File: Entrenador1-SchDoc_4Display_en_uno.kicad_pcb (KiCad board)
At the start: 2 copper layers, 154.9 x 106.7 mm, 85 parts, among them J11 CON8, J3 ICSP, J5 CON8, J6 CON8, J7 CON8, J9 3vias, P1 CONN_01X04, P10 CONN_01X04, P2 CONN_01X04, P3 CONN_01X05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

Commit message: Changes to be committed: 	modified:   Entrenador1-SchDoc_4Display_en_uno-cache.lib 	modified:   Entrenador1-SchDoc_4Display_en_uno.kicad_pcb 	modified:   Entrenador1-SchDoc_4Display_en_uno.kicad_pcb-bak 	modified:   Entrenador1-SchDoc_4Display_en_uno.sch 	modified:   Entrenador1-SchDoc_4Display_en_uno.sch-bak
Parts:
- moved R20 7.75 mm to (182.8, 60.5), turned to 270 degrees
- moved R26 7.62 mm to (189.6, 38.7), turned to 0 degrees
- moved R1 7.62 mm to (142.0, 106.7), turned to 90 degrees
- moved R17 7.62 mm to (142.9, 60.5), turned to 270 degrees
- moved R18 7.62 mm to (154.9, 60.5), turned to 270 degrees
- moved R19 7.62 mm to (171.8, 60.5), turned to 270 degrees
- moved R2 7.62 mm to (142.0, 109.2), turned to 270 degrees
- moved R21 7.62 mm to (189.6, 57.9), turned to 0 degrees
- moved R22 7.62 mm to (189.6, 42.5), turned to 0 degrees
- moved R23 7.62 mm to (189.6, 61.2), turned to 0 degrees
- moved R24 7.62 mm to (189.6, 46.3), turned to 0 degrees
- moved R25 7.62 mm to (187.3, 49.7), turned to 0 degrees
- moved R27 7.62 mm to (189.6, 54.6), turned to 0 degrees
- moved R28 7.62 mm to (189.6, 64.5), turned to 0 degrees
- moved R29 7.62 mm to (209.8, 63.8), turned to 0 degrees
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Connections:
- R1 pad 1: MCRL -> VDD
- R1 pad 2: VDD -> MCRL
- R17 pad 1: Disp1 -> Net-(Q1-Pad2)
- R17 pad 2: Net-(Q1-Pad2) -> Disp1
- R18 pad 1: Disp2 -> Net-(Q2-Pad2)
- R18 pad 2: Net-(Q2-Pad2) -> Disp2
- R19 pad 1: Disp3 -> Net-(Q3-Pad2)
- R19 pad 2: Net-(Q3-Pad2) -> Disp3
- R2 pad 1: RB4 -> VDD
- R2 pad 2: VDD -> RB4
- R20 pad 1: Disp4 -> Net-(Q4-Pad2)
- R20 pad 2: Net-(Q4-Pad2) -> Disp4
- R21 pad 1: Net-(R21-Pad1) -> /a
- R21 pad 2: /a -> Net-(R21-Pad2)
- R22 pad 1: Net-(R22-Pad1) -> /b
- R22 pad 2: /b -> Net-(R22-Pad2)
- R23 pad 1: Net-(R23-Pad1) -> /c
- R23 pad 2: /c -> Net-(R23-Pad2)
- R24 pad 1: Net-(R24-Pad1) -> /d
- R24 pad 2: /d -> Net-(R24-Pad2)
- R25 pad 1: Net-(R25-Pad1) -> /e
- R25 pad 2: /e -> Net-(R25-Pad2)
- R26 pad 1: Net-(R26-Pad1) -> /f
- R26 pad 2: /f -> Net-(R26-Pad2)
- R27 pad 1: Net-(R27-Pad1) -> /g
- R27 pad 2: /g -> Net-(R27-Pad2)
- R28 pad 1: /DisplayH -> /h
- R28 pad 2: /h -> /DisplayH
- R29 pad 1: GNDD -> /Display_A
- R29 pad 2: /Display_A -> GNDD
- R3 pad 1: Net-(D2-Pad1) -> RD0
- R3 pad 2: RD0 -> Net-(D2-Pad1)
- R30 pad 1: GNDD -> /Display_B
- R30 pad 2: /Display_B -> GNDD
- R31 pad 1: GNDD -> /Display_C
- R31 pad 2: /Display_C -> GNDD
- R32 pad 1: GNDD -> /Display_D
- R32 pad 2: /Display_D -> GNDD
- R4 pad 1: Net-(D3-Pad1) -> RD1
- R4 pad 2: RD1 -> Net-(D3-Pad1)
- R7 pad 1: VDD -> Boton3
- R7 pad 2: Boton3 -> VDD
- R8 pad 1: VDD -> Boton4
- R8 pad 2: Boton4 -> VDD
- U3 pad 10: Net-(R24-Pad1) -> Net-(R24-Pad2)
- U3 pad 11: Net-(R23-Pad1) -> Net-(R23-Pad2)
- U3 pad 12: Net-(R22-Pad1) -> Net-(R22-Pad2)
- U3 pad 13: Net-(R21-Pad1) -> Net-(R21-Pad2)
- U3 pad 14: Net-(R27-Pad1) -> Net-(R27-Pad2)
- U3 pad 15: Net-(R26-Pad1) -> Net-(R26-Pad2)
- U3 pad 9: Net-(R25-Pad1) -> Net-(R25-Pad2)
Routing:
- net Net-(R23-Pad2): track 0.00 -> 26.5 mm
- net Net-(R23-Pad1): track 26.5 -> 0.00 mm
- net Net-(R25-Pad2): track 0.00 -> 22.4 mm
- net Net-(R25-Pad1): track 22.4 -> 0.00 mm
- net Net-(R26-Pad2): track 0.00 -> 20.0 mm
- net Net-(R26-Pad1): track 20.0 -> 0.00 mm
- net Net-(R21-Pad2): track 0.00 -> 19.4 mm
- net Net-(R21-Pad1): track 19.4 -> 0.00 mm
- net Net-(R27-Pad2): track 0.00 -> 15.1 mm
- net Net-(R27-Pad1): track 15.1 -> 0.00 mm
- net Net-(R24-Pad2): track 0.00 -> 12.3 mm
- net Net-(R24-Pad1): track 12.3 -> 0.00 mm
- net Net-(R22-Pad2): track 0.00 -> 6.70 mm
- net Net-(R22-Pad1): track 6.70 -> 0.00 mm

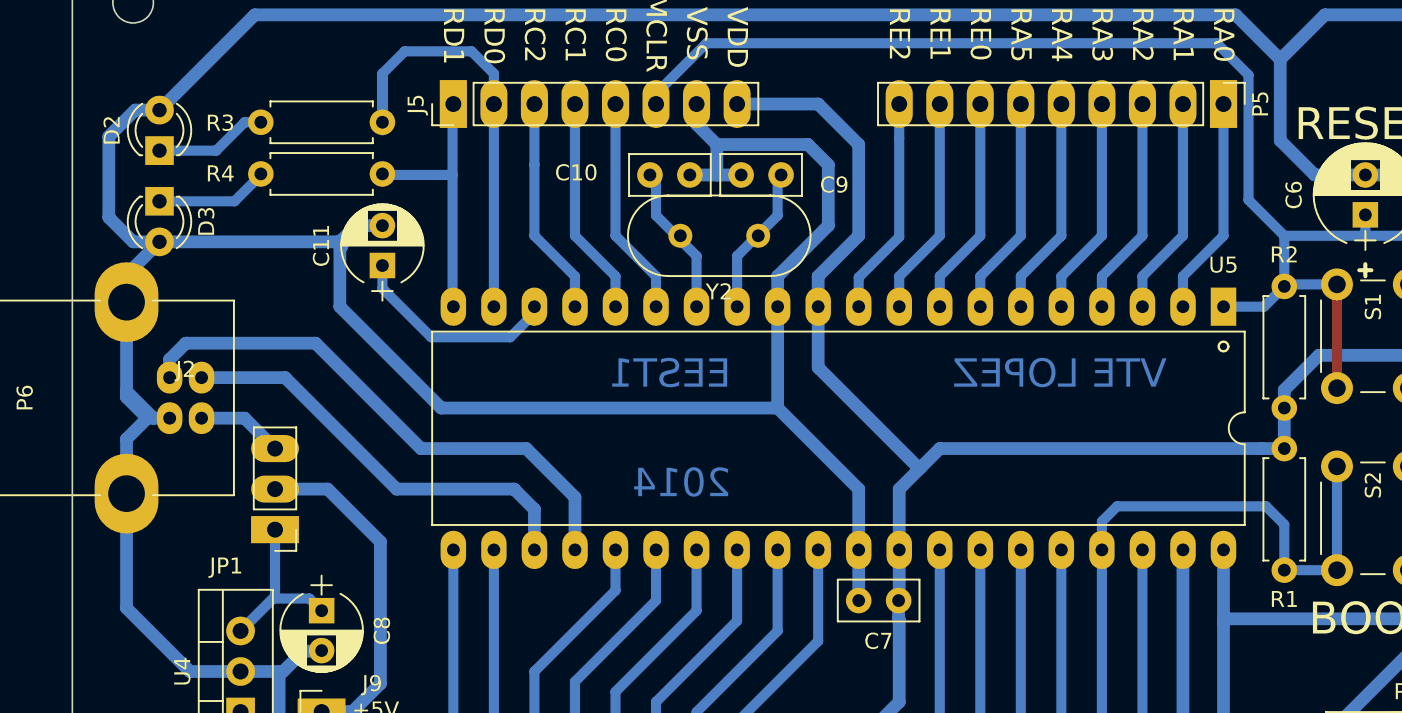
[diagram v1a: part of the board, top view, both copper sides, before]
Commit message: modified:   Entrenador1-SchDoc_4Display_en_uno-cache.lib 	modified:   Entrenador1-SchDoc_4Display_en_uno.kicad_pcb 	modified:   Entrenador1-SchDoc_4Display_en_uno.kicad_pcb-bak 	modified:   Entrenador1-SchDoc_4Display_en_uno.net 	modified:   Entrenador1-SchDoc_4Display_en_uno.sch 	modified:   Entrenador1-SchDoc_4Display_en_uno.sch-bak 	modified:   fp-info-cache 	renamed:    Entrenador1-SchDoc-cache.lib -> lib_sch/Entrenador1-SchDoc-cache.lib 	renamed:    Entrenador1-SchDoc-rescue.lib -> lib_sch/Entrenador1-SchDoc-rescue.lib 	new file:   lib_sch/Entrenador1-SchDoc_4Display_en_uno.bck 	new file:   lib_sch/Entrenador1-SchDoc_4Display_en_uno.dcm 	new file:   lib_sch/Entrenador1-SchDoc_4Display_en_uno.lib 	modified:   sym-lib-table
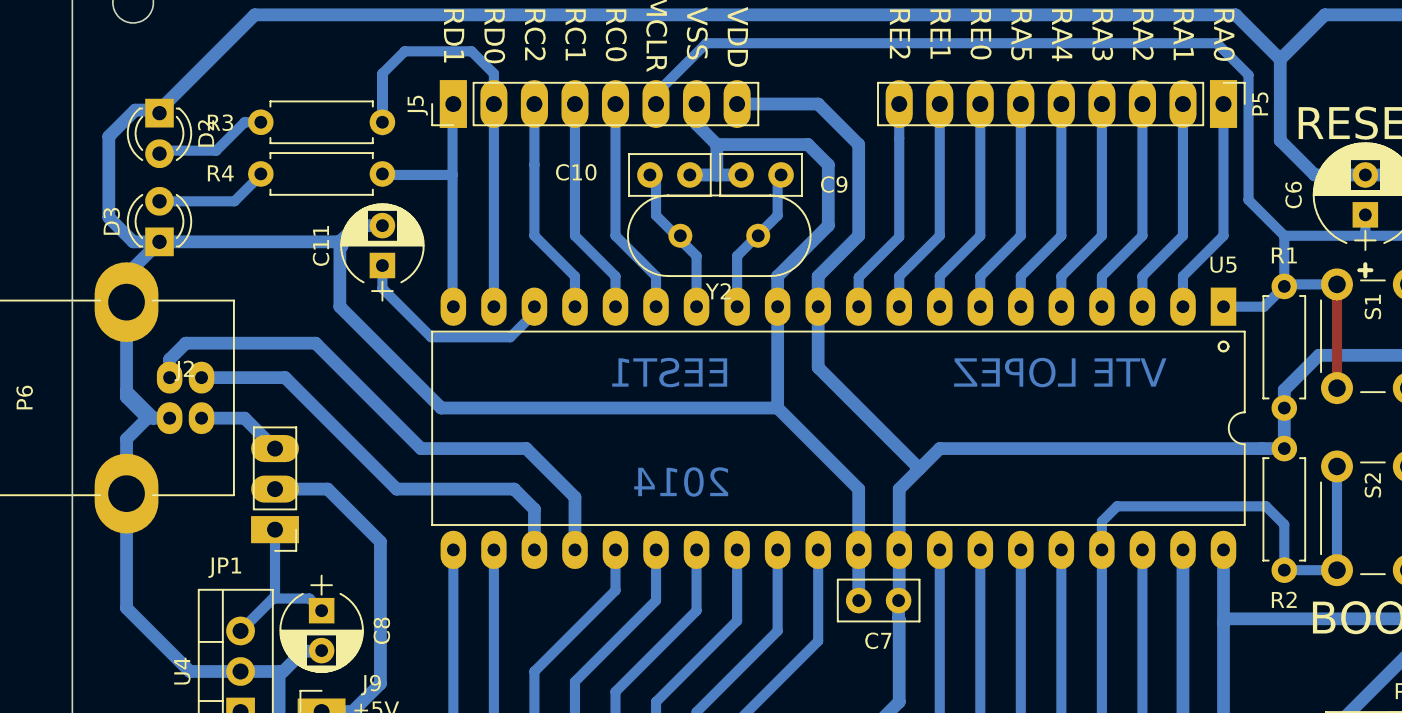
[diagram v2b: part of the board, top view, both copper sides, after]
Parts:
- moved R1 7.62 mm to (142.0, 99.1), turned to 270 degrees
- moved R2 7.62 mm to (142.0, 116.8), turned to 90 degrees
- moved D3 2.54 mm to (71.5, 96.3), turned to 90 degrees
- moved D2 2.35 mm to (71.5, 88.2), turned to 270 degrees
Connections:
- net +12VFuente renamed Net-(D12-Pad2)
- net +5VFuente renamed /+5VFuente
- D2 pad 1: Net-(D2-Pad1) -> GND
- D2 pad 2: GND -> Net-(D2-Pad2)
- D3 pad 1: Net-(D3-Pad1) -> GND
- D3 pad 2: GND -> Net-(D3-Pad2)
- R1 pad 1: VDD -> MCRL
- R1 pad 2: MCRL -> VDD
- R2 pad 1: VDD -> RB4
- R2 pad 2: RB4 -> VDD
- R3 pad 2: Net-(D2-Pad1) -> Net-(D2-Pad2)
- R4 pad 2: Net-(D3-Pad1) -> Net-(D3-Pad2)
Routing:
- net Net-(D2-Pad2): track 0.00 -> 7.09 mm
- net Net-(D2-Pad1): track 7.09 -> 0.00 mm
- net Net-(D3-Pad2): track 0.00 -> 7.03 mm
- net Net-(D3-Pad1): track 7.03 -> 0.00 mm

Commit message: Changes to be committed: 	new file:   Circuito2.sch 	deleted:    "Documentaci\303\263n/2020/.~lock.ListaComponentes.csv#" 	modified:   "Documentaci\303\263n/2020/Armado.aux" 	modified:   "Documentaci\303\263n/2020/Armado.tex" 	modified:   "Documentaci\303\263n/2020/Introduccion.aux" 	modified:   "Documentaci\303\263n/2020/Principal.aux" 	modified:   "Documentaci\303\263n/2020/Principal.log" 	modified:   "Documentaci\303\263n/2020/Principal.pdf" 	modified:   "Documentaci\303\263n/2020/Principal.synctex.gz" 	modified:   "Documentaci\303\263n/2020/Principal.tex" 	modified:   "Documentaci\303\263n/2020/Principal.toc" 	new file:   "Documentaci\303\263n/2020/imagenes/logo2.jpg" 	deleted:    Entrenador1-SchDoc.csv 	deleted:    Entrenador1-SchDoc_4Display_en_uno (2).csv 	deleted:    Entrenador1-SchDoc_4Display_en_uno.csv 	modified:   Entrenador1-SchDoc_4Display_en_uno.kicad_pcb 	modified:   Entrenador1-SchDoc_4Display_en_uno.kicad_pcb-bak 	modified:   Entrenador1-SchDoc_4Display_en_uno.pro 	modified:   Entrenador1-SchDoc_4Display_en_uno.sch 	modified:   Entrenador1-SchDoc_4Display_en_uno.sch-bak 	deleted:    Gabinete/Base.FCStd 	deleted:    Gabinete/Base.FCStd1 	deleted:    Gabinete/Base.step 	deleted:    Gabinete/Entrenador1-SchDoc.step 	deleted:    Gabinete/Entrenador1-SchDoc1.step 	deleted:    Gabinete/Entrenador1_SchDoc.FCStd1 	deleted:    Gabinete/PlanoGabinete.pdf 	deleted:    Gabinete/frente.FCStd 	deleted:    Gabinete/frente.FCStd1 	deleted:    Gabinete/frente1.step 	deleted:    ImagenesCapturadas/Entrenador1-SchDoc.jpg 	deleted:    ImagenesCapturadas/Entrenador1-SchDoc.png 	deleted:    ImagenesCapturadas/Entrenador1-SchDoc_4Display_en_uno.png 	deleted:    _autosave-Entrenador1-SchDoc_4Display_en_uno.kicad_pcb 	new file:   _autosave-file5E8BEFED.sch
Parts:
- J11: value CON8 -> LEDS
- P10: value CONN_01X04 -> Negativo
- P2: value CONN_01X04 -> DISPLAY
- P4: value CONN_01X04 -> BOTONES
- P7: value CONN_01X02 -> 12V
- P8: value CONN_01X02 -> 5V
- P9: value CONN_01X04 -> Positivo
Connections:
- net Net-(P1-Pad2) renamed VA2
- net Net-(P1-Pad3) renamed VA1

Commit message: Changes to be committed: 	deleted:    Circuito2.sch 	modified:   "Documentaci\303\263n/2020/Armado.aux" 	modified:   "Documentaci\303\263n/2020/Armado.tex" 	modified:   "Documentaci\303\263n/2020/Principal.aux" 	modified:   "Documentaci\303\263n/2020/Principal.log" 	modified:   "Documentaci\303\263n/2020/Principal.pdf" 	modified:   "Documentaci\303\263n/2020/Principal.synctex.gz" 	deleted:    "Documentaci\303\263n/2020/Pr\303\241cticas.log" 	deleted:    "Documentaci\303\263n/2020/Pr\303\241cticas.tex" 	deleted:    "Documentaci\303\263n/2020/Puesta en Marcha.tex" 	modified:   "Documentaci\303\263n/2020/imagenes/ComponentesEntrenador.pdf"
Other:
- board text added: "+5V 7805"
- board text added: "+5VUSB"
- board text added: "+5V_VDD"
- board text added: "A"
- board text added: "B"
- board text added: "B1"
- board text added: "B2"
- board text added: "B3"
- board text added: "B4"
- board text added: "C"
- board text added: "D"
- board text added: "Fuente (+12V)"
- board text added: "Fuente (+5V)"
- board text added: "H"
- board text added: "LEDs"
- board text added: "VA1"
- board text added: "VA2"
- board text added: "Vref A+"
- board text added: "Vref A-"
- board text removed: "J1"

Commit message: Changes to be committed: 	new file:   CAM/Entrenador2020.FlatPrj 	new file:   "Documentaci\303\263n/2020/CAM_AcrilicoEntrenador_2.nc" 	new file:   "Documentaci\303\263n/2020/CAM_AcrilicoEntrenador_3.nc" 	modified:   Entrenador1-SchDoc_4Display_en_uno-cache.lib 	modified:   Entrenador1-SchDoc_4Display_en_uno.kicad_pcb 	modified:   Entrenador1-SchDoc_4Display_en_uno.kicad_pcb-bak 	modified:   Entrenador1-SchDoc_4Display_en_uno.net 	modified:   Entrenador1-SchDoc_4Display_en_uno.sch 	modified:   Entrenador1-SchDoc_4Display_en_uno.sch-bak 	new file:   Film/Entrenador1-SchDoc_4Display_en_uno-B_Cu.gbr_panelized.svg 	new file:   Film/Entrenador1-SchDoc_4Display_en_uno-Edge_Cuts.gbr_panelized.svg 	new file:   GerberOutput/Entrenador1-SchDoc_4Display_en_uno-B_Cu.gbr 	new file:   GerberOutput/Entrenador1-SchDoc_4Display_en_uno-Edge_Cuts.gbr 	new file:   GerberOutput/Entrenador1-SchDoc_4Display_en_uno-drl.rpt 	new file:   GerberOutput/Entrenador1-SchDoc_4Display_en_uno-drl_map.gbr 	new file:   GerberOutput/Entrenador1-SchDoc_4Display_en_uno.drl 	modified:   fp-info-cache
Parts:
- added H1: MountingHole, Mounting_Holes:MountingHole_3.2mm_M3, F.Cu at (69.8, 36.8)
- added H2: MountingHole, Mounting_Holes:MountingHole_3.2mm_M3, F.Cu at (217.2, 36.8)
- added H3: MountingHole, Mounting_Holes:MountingHole_3.2mm_M3, F.Cu at (69.8, 69.2)
- added H4: MountingHole, Mounting_Holes:MountingHole_3.2mm_M3, F.Cu at (217.2, 69.2)
- added H5: MountingHole, Mounting_Holes:MountingHole_3.2mm_M3, F.Cu at (217.2, 81.3)
- added H6: MountingHole, Mounting_Holes:MountingHole_3.2mm_M3, F.Cu at (217.2, 135.9)
- added H7: MountingHole, Mounting_Holes:MountingHole_3.2mm_M3, F.Cu at (69.8, 80.6)
- added H8: MountingHole, Mounting_Holes:MountingHole_3.2mm_M3, F.Cu at (69.8, 135.9)
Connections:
- C10 pad 2: GND -> Net-(C10-Pad2)
- C9 pad 2: GND -> Net-(C9-Pad2)
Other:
- outline, holes or cut-outs redrawn
